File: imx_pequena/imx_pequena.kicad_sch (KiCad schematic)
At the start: 0 parts

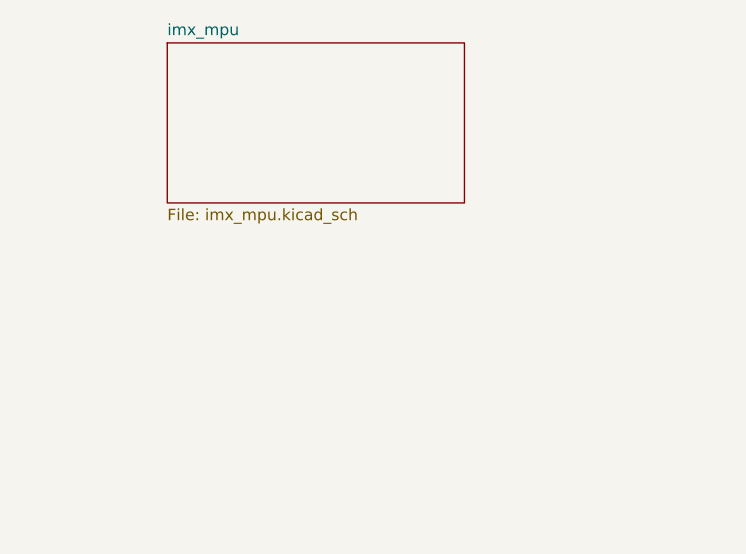
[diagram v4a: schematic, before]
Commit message: USB Updates
Back in the saddle after moving. Added USB C and USB OTG symbols and supporting passives.
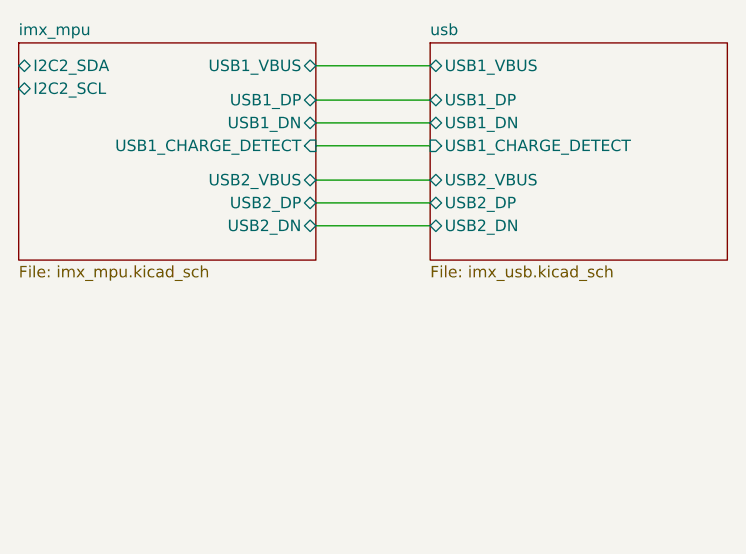
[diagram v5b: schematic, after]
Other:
- added sheet usb (imx_usb.kicad_sch)
- sheet imx_mpu ports: added I2C2_SCL, I2C2_SDA, USB1_CHARGE_DETECT, USB1_DN, USB1_DP, USB1_VBUS, USB2_DN, USB2_DP, USB2_VBUS; removed none

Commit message: Power Update
Added 3v3 and 1.35V switchers
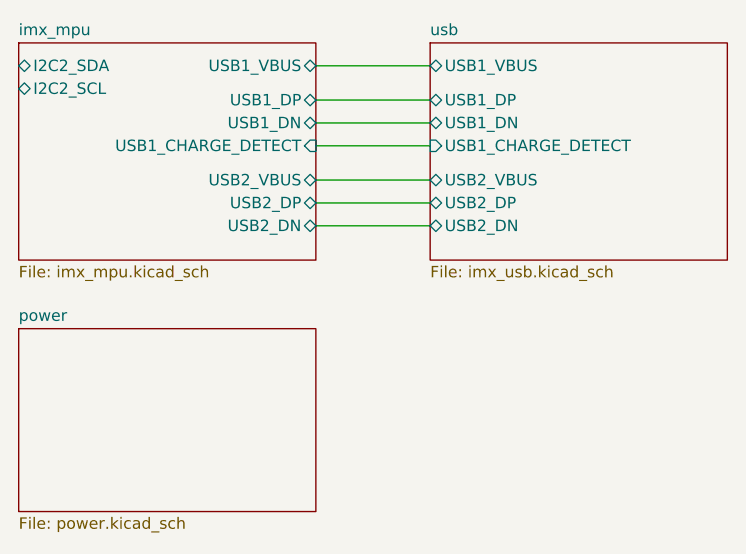
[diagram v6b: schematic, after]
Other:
- added sheet power (power.kicad_sch)
